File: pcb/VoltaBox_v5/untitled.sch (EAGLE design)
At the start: 59 parts, among them X1 112J-TDAR-R(MICROSD), X2 52892-0895, X3 52892-0895, X4 XT30PW-F, X6 XT60PW-M, X7 1050170001

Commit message: pre final
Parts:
- added J1: 0, rcl:R-EU_R2010
- X7: value 1050170001 -> KLS1-233; device 1050170001:1050170001 -> untitled:KLS1-233
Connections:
- net +12V: now also J1.1
- net +4V: now also J1.2
- net D_N: now also X7.P$2; no longer X7.2
- net D_P: now also X7.P$3; no longer X7.3
- net GND: now also X7.P$5, X7.P$6; no longer X7.5, X7.SHIELD
- net VCC: now also X7.P$1; no longer X7.1
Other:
- note removed: "ЗАМЕНИТЬ"
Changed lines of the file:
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@@
 <part name="C23" library="rcl" library_urn="urn:adsk.eagle:library:334" deviceset="C-EU" device="C2220K" package3d_urn="urn:adsk.eagle:package:23687/2" value="4.7u"/>
 <part name="GND14" library="supply1" library_urn="urn:adsk.eagle:library:371" deviceset="GND" device=""/>
-<part name="X7" library="1050170001" deviceset="1050170001" device=""/>
 <part name="C21" library="rcl" library_urn="urn:adsk.eagle:library:334" deviceset="CPOL-US" device="150CLZ-1014" package3d_urn="urn:adsk.eagle:package:23405/1" value="100u"/>
 <part name="D1" library="untitled" deviceset="STPS5L60S" device=""/>
@@
 <part name="X4" library="untitled" deviceset="XT30PW-F" device=""/>
 <part name="U$6" library="untitled" deviceset="+4V" device=""/>
+<part name="J1" library="rcl" library_urn="urn:adsk.eagle:library:334" deviceset="R-EU_" device="R2010" package3d_urn="urn:adsk.eagle:package:23551/2" value="0"/>
+<part name="X7" library="untitled" deviceset="KLS1-233" device=""/>
 </parts>
 <sheets>
@@
 <text x="152.4" y="29.21" size="1.778" layer="91">GND</text>
 <text x="152.4" y="46.99" size="1.778" layer="91">+3V</text>
-<text x="154.94" y="81.28" size="1.778" layer="91">ЗАМЕНИТЬ</text>
 </plain>
 <instances>
@@
 <instance part="GND13" gate="1" x="25.4" y="96.52"/>
 <instance part="GND15" gate="1" x="81.28" y="119.38"/>
-<instance part="GND16" gate="1" x="137.16" y="66.04"/>
+<instance part="GND16" gate="1" x="137.16" y="68.58"/>
 <instance part="GND17" gate="1" x="96.52" y="38.1"/>
 <instance part="X1" gate="G$1" x="86.36" y="149.86"/>
@@
 <instance part="C9" gate="G$1" x="190.5" y="149.86"/>
 <instance part="GND14" gate="1" x="33.02" y="124.46"/>
-<instance part="X7" gate="G$1" x="154.94" y="76.2" rot="MR0"/>
+<instance part="X7" gate="G$1" x="165.1" y="78.74"/>
 </instances>
 <busses>
@@
 <segment>
 <wire x1="144.78" y1="73.66" x2="137.16" y2="73.66" width="0.1524" layer="91"/>
-<wire x1="137.16" y1="73.66" x2="137.16" y2="68.58" width="0.1524" layer="91"/>
-<wire x1="137.16" y1="68.58" x2="144.78" y2="68.58" width="0.1524" layer="91"/>
+<wire x1="137.16" y1="73.66" x2="137.16" y2="71.12" width="0.1524" layer="91"/>
+<wire x1="137.16" y1="71.12" x2="144.78" y2="71.12" width="0.1524" layer="91"/>
 <pinref part="GND16" gate="1" pin="GND"/>
-<junction x="137.16" y="68.58"/>
+<junction x="137.16" y="71.12"/>
 <label x="137.16" y="76.2" size="1.778" layer="95"/>
-<pinref part="X7" gate="G$1" pin="5"/>
-<pinref part="X7" gate="G$1" pin="SHIELD"/>
+<pinref part="X7" gate="G$1" pin="P$5"/>
+<pinref part="X7" gate="G$1" pin="P$6"/>
 </segment>
 <segment>
@@
 <junction x="137.16" y="88.9"/>
 <label x="137.16" y="83.82" size="1.778" layer="95"/>
-<pinref part="X7" gate="G$1" pin="1"/>
+<pinref part="X7" gate="G$1" pin="P$1"/>
 </segment>
 </net>
@@
 <wire x1="121.92" y1="81.28" x2="144.78" y2="81.28" width="0.1524" layer="91"/>
 <label x="137.16" y="81.28" size="1.778" layer="95"/>
-<pinref part="X7" gate="G$1" pin="2"/>
+<pinref part="X7" gate="G$1" pin="P$2"/>
 </segment>
 </net>
@@
 <junction x="124.46" y="78.74"/>
 <label x="137.16" y="78.74" size="1.778" layer="95"/>
-<pinref part="X7" gate="G$1" pin="3"/>
+<pinref part="X7" gate="G$1" pin="P$3"/>
 </segment>
 </net>
@@
 <instance part="DA3" gate="G$1" x="152.4" y="-17.78"/>
 <instance part="R3" gate="G$1" x="127" y="10.16"/>
-<instance part="U$12" gate="G$1" x="101.6" y="38.1"/>
+<instance part="U$12" gate="G$1" x="101.6" y="48.26"/>
 <instance part="U$11" gate="G$1" x="170.18" y="-35.56"/>
 <instance part="DA2" gate="G$1" x="35.56" y="-22.86"/>
@@
 <instance part="X4" gate="G$1" x="142.24" y="22.86"/>
 <instance part="U$6" gate="G$1" x="142.24" y="25.4"/>
+<instance part="J1" gate="G$1" x="73.66" y="43.18"/>
 </instances>
 <busses>
@@
 <pinref part="C23" gate="G$1" pin="1"/>
 <junction x="-2.54" y="45.72"/>
+<pinref part="J1" gate="G$1" pin="1"/>
+<wire x1="40.64" y1="45.72" x2="68.58" y2="45.72" width="0.1524" layer="91"/>
+<wire x1="68.58" y1="45.72" x2="68.58" y2="43.18" width="0.1524" layer="91"/>
+<junction x="40.64" y="45.72"/>
 </segment>
 <segment>
@@
 <wire x1="83.82" y1="17.78" x2="86.36" y2="17.78" width="0.1524" layer="91"/>
 <pinref part="R4" gate="G$1" pin="1"/>
-<wire x1="86.36" y1="17.78" x2="86.36" y2="0" width="0.1524" layer="91"/>
-<wire x1="86.36" y1="0" x2="106.68" y2="0" width="0.1524" layer="91"/>
-<junction x="86.36" y="17.78"/>
 <pinref part="DA1" gate="G$1" pin="PG"/>
 </segment>
@@
 <junction x="86.36" y="30.48"/>
 <pinref part="U$12" gate="G$1" pin="+4V"/>
-<wire x1="101.6" y1="30.48" x2="101.6" y2="35.56" width="0.1524" layer="91"/>
+<wire x1="101.6" y1="30.48" x2="101.6" y2="43.18" width="0.1524" layer="91"/>
 <junction x="101.6" y="30.48"/>
 <pinref part="L1" gate="G$1" pin="2"/>
 <pinref part="C21" gate="G$1" pin="+"/>
-</segment>
-<segment>
+<pinref part="J1" gate="G$1" pin="2"/>
+<wire x1="101.6" y1="43.18" x2="101.6" y2="45.72" width="0.1524" layer="91"/>
+<wire x1="78.74" y1="43.18" x2="101.6" y2="43.18" width="0.1524" layer="91"/>
+<junction x="101.6" y="43.18"/>
+</segment>
+<segment>

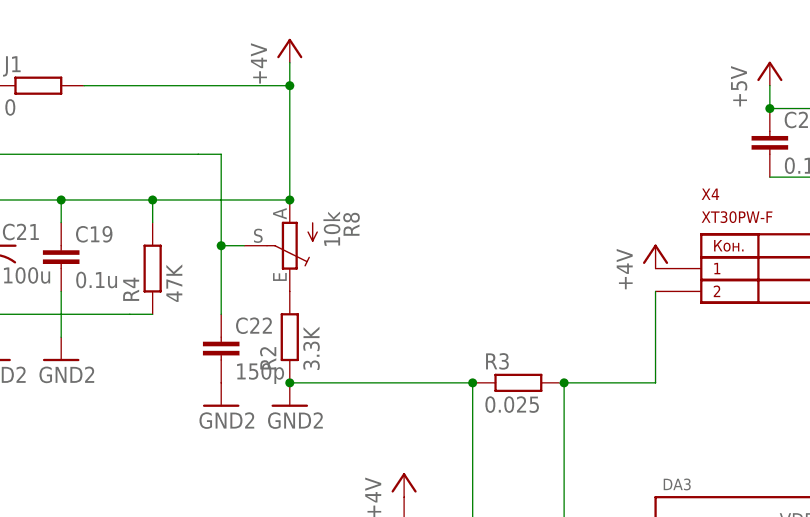
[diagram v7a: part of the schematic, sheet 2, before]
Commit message: Put some silk to the it's places. Added 3 testpoints.
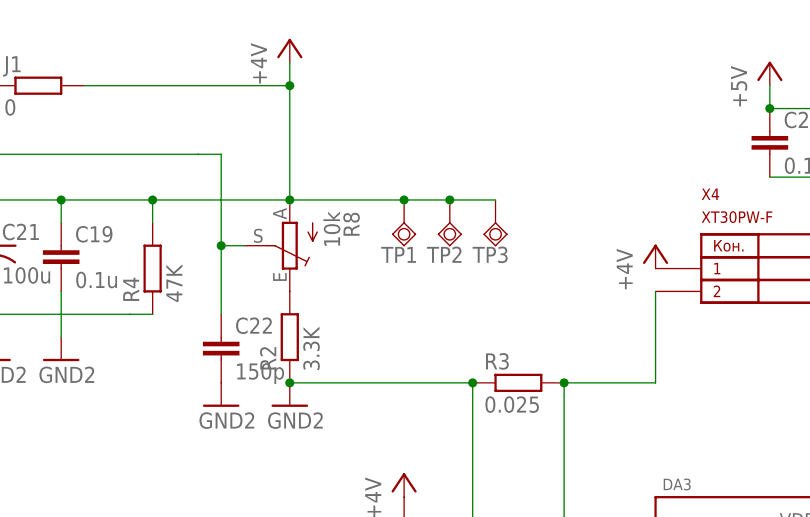
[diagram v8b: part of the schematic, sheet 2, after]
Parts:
- added TP1, TP2, TP3: TPSQB1,27, testpad:TPSQB1,27
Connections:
- net +4V: now also TP1.TP, TP2.TP, TP3.TP
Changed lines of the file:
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@@
 <part name="J1" library="rcl" library_urn="urn:adsk.eagle:library:334" deviceset="R-EU_" device="R2010" package3d_urn="urn:adsk.eagle:package:23551/2" value="0"/>
 <part name="X7" library="untitled" deviceset="KLS1-233" device=""/>
+<part name="TP1" library="testpad" library_urn="urn:adsk.eagle:library:385" deviceset="TPSQ" device="B1,27" package3d_urn="urn:adsk.eagle:package:27944/1"/>
+<part name="TP2" library="testpad" library_urn="urn:adsk.eagle:library:385" deviceset="TPSQ" device="B1,27" package3d_urn="urn:adsk.eagle:package:27944/1"/>
+<part name="TP3" library="testpad" library_urn="urn:adsk.eagle:library:385" deviceset="TPSQ" device="B1,27" package3d_urn="urn:adsk.eagle:package:27944/1"/>
 </parts>
 <sheets>
@@
 <instance part="U$6" gate="G$1" x="142.24" y="25.4"/>
 <instance part="J1" gate="G$1" x="73.66" y="43.18"/>
+<instance part="TP1" gate="G$1" x="114.3" y="27.94"/>
+<instance part="TP2" gate="G$1" x="119.38" y="27.94"/>
+<instance part="TP3" gate="G$1" x="124.46" y="27.94"/>
 </instances>
 <busses>
@@
 <wire x1="78.74" y1="43.18" x2="101.6" y2="43.18" width="0.1524" layer="91"/>
 <junction x="101.6" y="43.18"/>
-</segment>
-<segment>
+<pinref part="TP1" gate="G$1" pin="TP"/>
+<wire x1="101.6" y1="30.48" x2="114.3" y2="30.48" width="0.1524" layer="91"/>
+<pinref part="TP2" gate="G$1" pin="TP"/>
+<wire x1="119.38" y1="30.48" x2="114.3" y2="30.48" width="0.1524" layer="91"/>
+<junction x="114.3" y="30.48"/>
+<pinref part="TP3" gate="G$1" pin="TP"/>
+<wire x1="124.46" y1="30.48" x2="119.38" y2="30.48" width="0.1524" layer="91"/>
+<junction x="119.38" y="30.48"/>
+</segment>
+<segment>
